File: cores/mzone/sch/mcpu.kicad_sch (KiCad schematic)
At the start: 36 parts

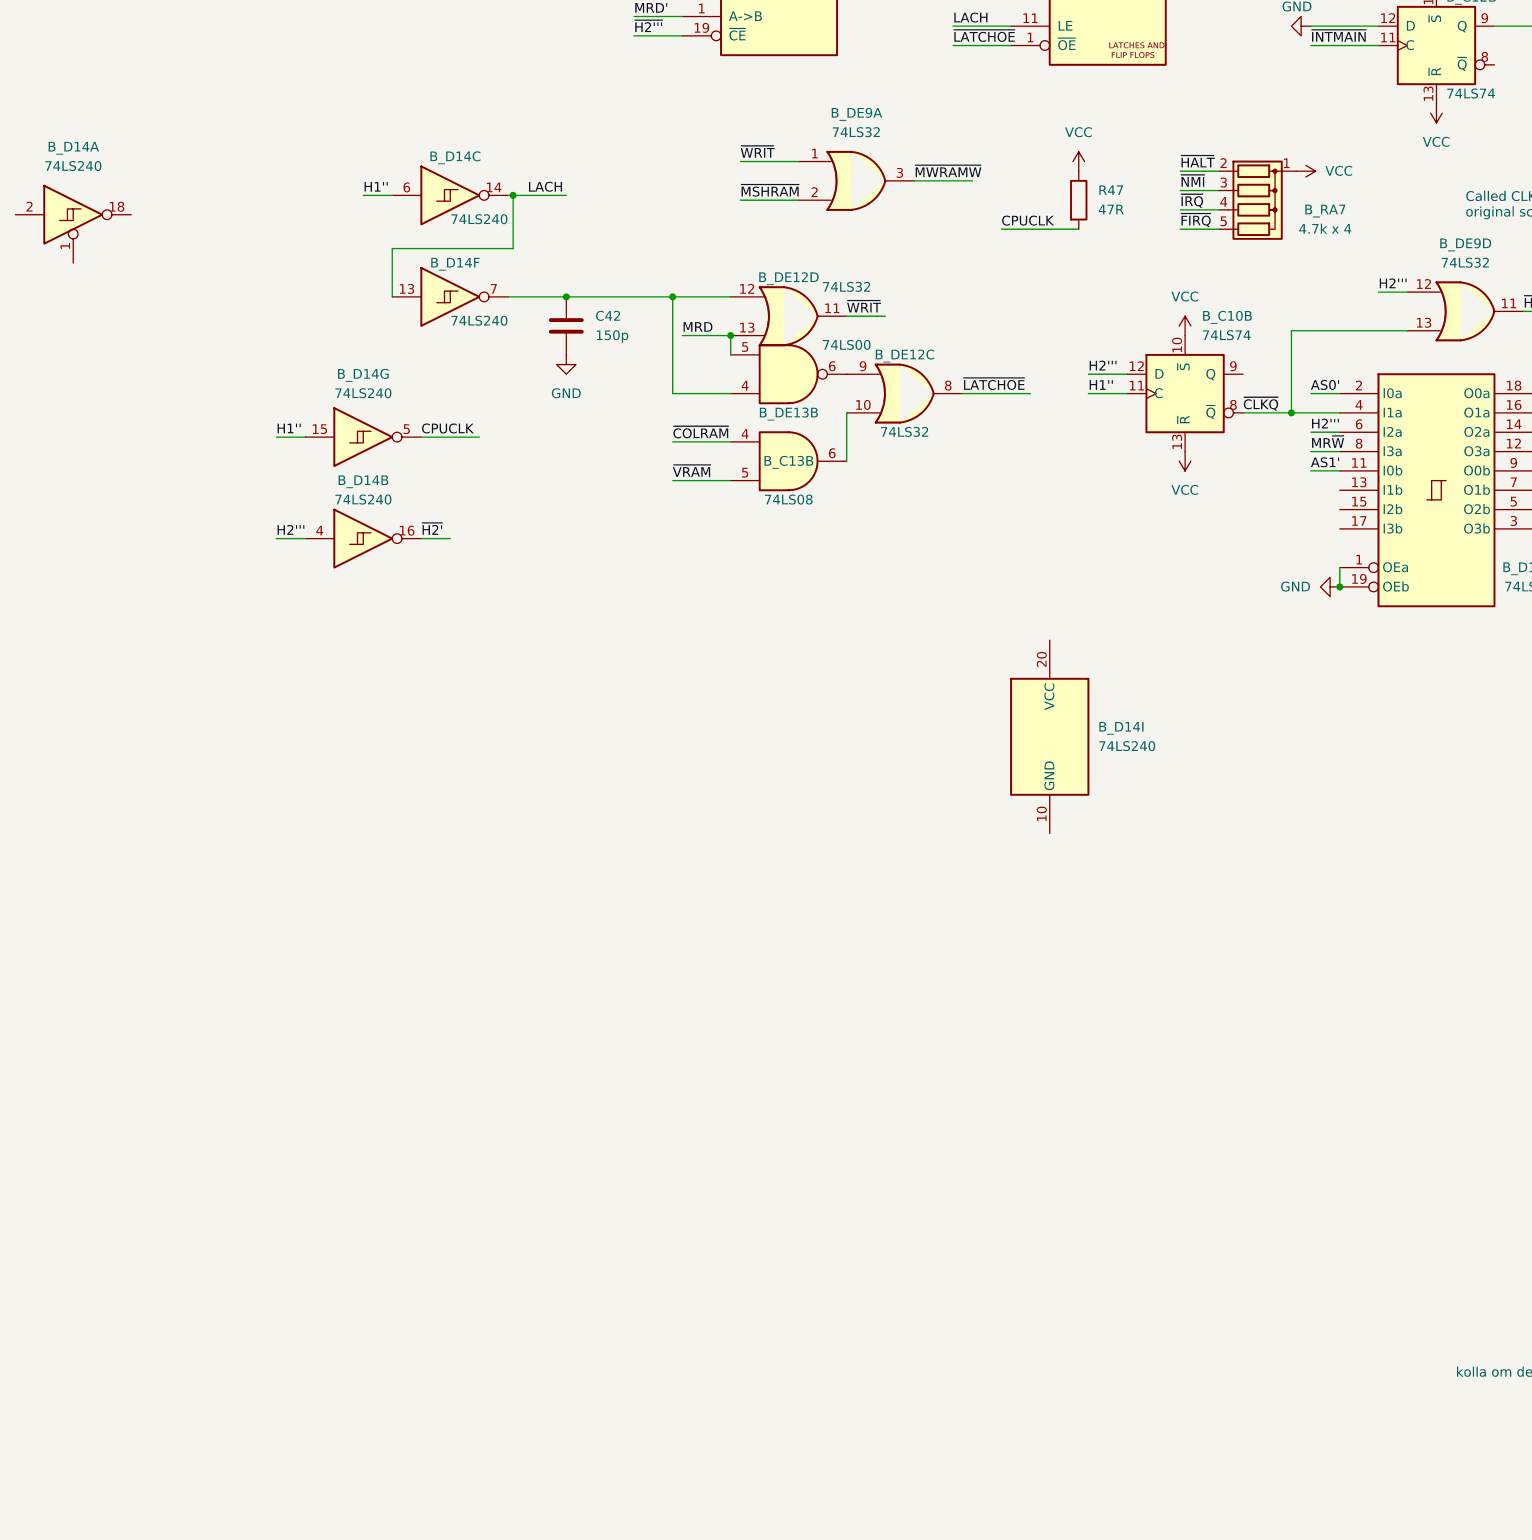
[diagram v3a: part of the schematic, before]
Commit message: mzone core
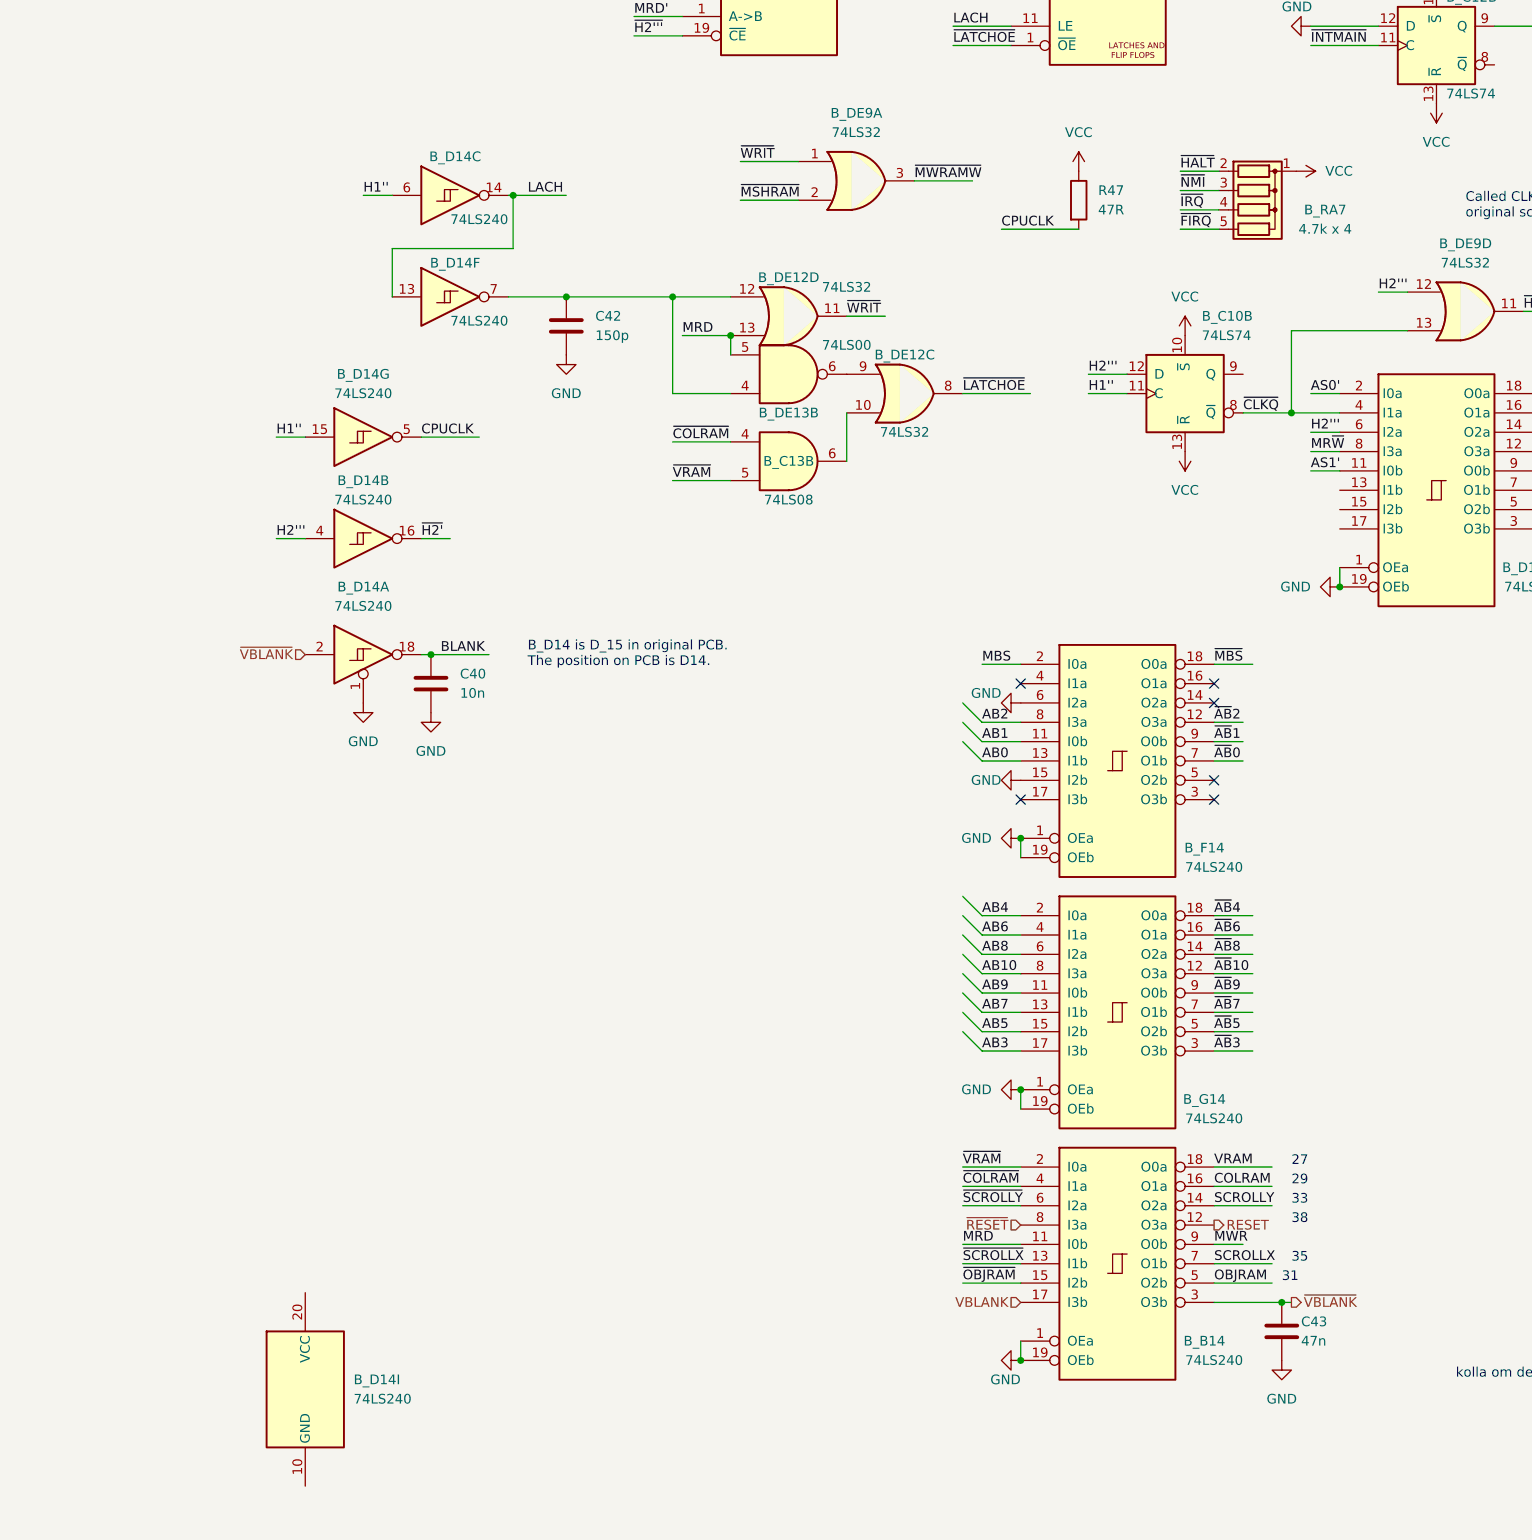
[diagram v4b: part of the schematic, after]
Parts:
- added B_B14, B_F14, B_G14: 74LS240, symbol jt74:74LS240
- added C40: 10n, symbol Device:C
- added C43: 47n, symbol Device:C
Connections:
- net AB0: now also B_F14.13 (I1b)
- net AB1: now also B_F14.11 (I0b)
- net AB10: now also B_G14.8 (I3a)
- net AB2: now also B_F14.8 (I3a)
- net AB3: now also B_G14.17 (I3b)
- net AB4: now also B_G14.2 (I0a)
- net AB5: now also B_G14.15 (I2b)
- net AB6: now also B_G14.4 (I1a)
- net AB7: now also B_G14.13 (I1b)
- net AB8: now also B_G14.6 (I2a)
- net AB9: now also B_G14.11 (I0b)
- net BLANK: now also B_D14.18, C40.1
- net GND: now also B_D14.1, B_B14.1 (OEa), B_B14.19 (OEb), B_F14.1 (OEa), B_F14.15 (I2b), B_F14.19 (OEb), B_F14.6 (I2a), B_G14.1 (OEa), B_G14.19 (OEb), C40.2, C43.2
- net MBS: now also B_F14.2 (I0a)
- net MRD: now also B_B14.11 (I0b)
- net VCC: now also B_B14.20 (VCC), B_F14.20 (VCC), B_G14.20 (VCC)
- net VSS: now also B_B14.10 (VSS), B_F14.10 (VSS), B_G14.10 (VSS)
- net ~{COLRAM}: now also B_B14.4 (I1a)
- net ~{MBS}: now also B_F14.18 (O0a)
- net ~{OBJRAM}: now also B_B14.15 (I2b)
- net ~{RESET}: now also B_B14.8 (I3a)
- net ~{SCROLLX}: now also B_B14.13 (I1b)
- net ~{SCROLLY}: now also B_B14.6 (I2a)
- net ~{VRAM}: now also B_B14.2 (I0a)
- net ~{VBLANK}: now reaches B_D14.2
- net ~{VBLANK}: now also B_B14.3 (O3b), C43.1
- new net COLRAM: B_B14.16 (O1a)
- new net MWR: B_B14.9 (O0b)
- new net OBJRAM: B_B14.5 (O2b)
- new net RESET: B_B14.12 (O3a)
- new net SCROLLX: B_B14.7 (O1b)
- new net SCROLLY: B_B14.14 (O2a)
- new net VBLANK: B_B14.17 (I3b)
- new net VRAM: B_B14.18 (O0a)
- new net ~{AB}0: B_F14.7 (O1b)
- new net ~{AB}1: B_F14.9 (O0b)
- new net ~{AB}10: B_G14.12 (O3a)
- new net ~{AB}2: B_F14.12 (O3a)
- new net ~{AB}3: B_G14.3 (O3b)
- new net ~{AB}4: B_G14.18 (O0a)
- new net ~{AB}5: B_G14.5 (O2b)
- new net ~{AB}6: B_G14.16 (O1a)
- new net ~{AB}7: B_G14.7 (O1b)
- new net ~{AB}8: B_G14.14 (O2a)
- new net ~{AB}9: B_G14.9 (O0b)
- no-connect marks 7 -> 13
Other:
- note added: "27"
- note added: "29"
- note added: "31"
- note added: "33"
- note added: "35"
- note added: "38"
- note added: "B_D14 is D_15 in original PCB. The position on PCB is D14."
- moved on the sheet: B_D14A, B_D14I

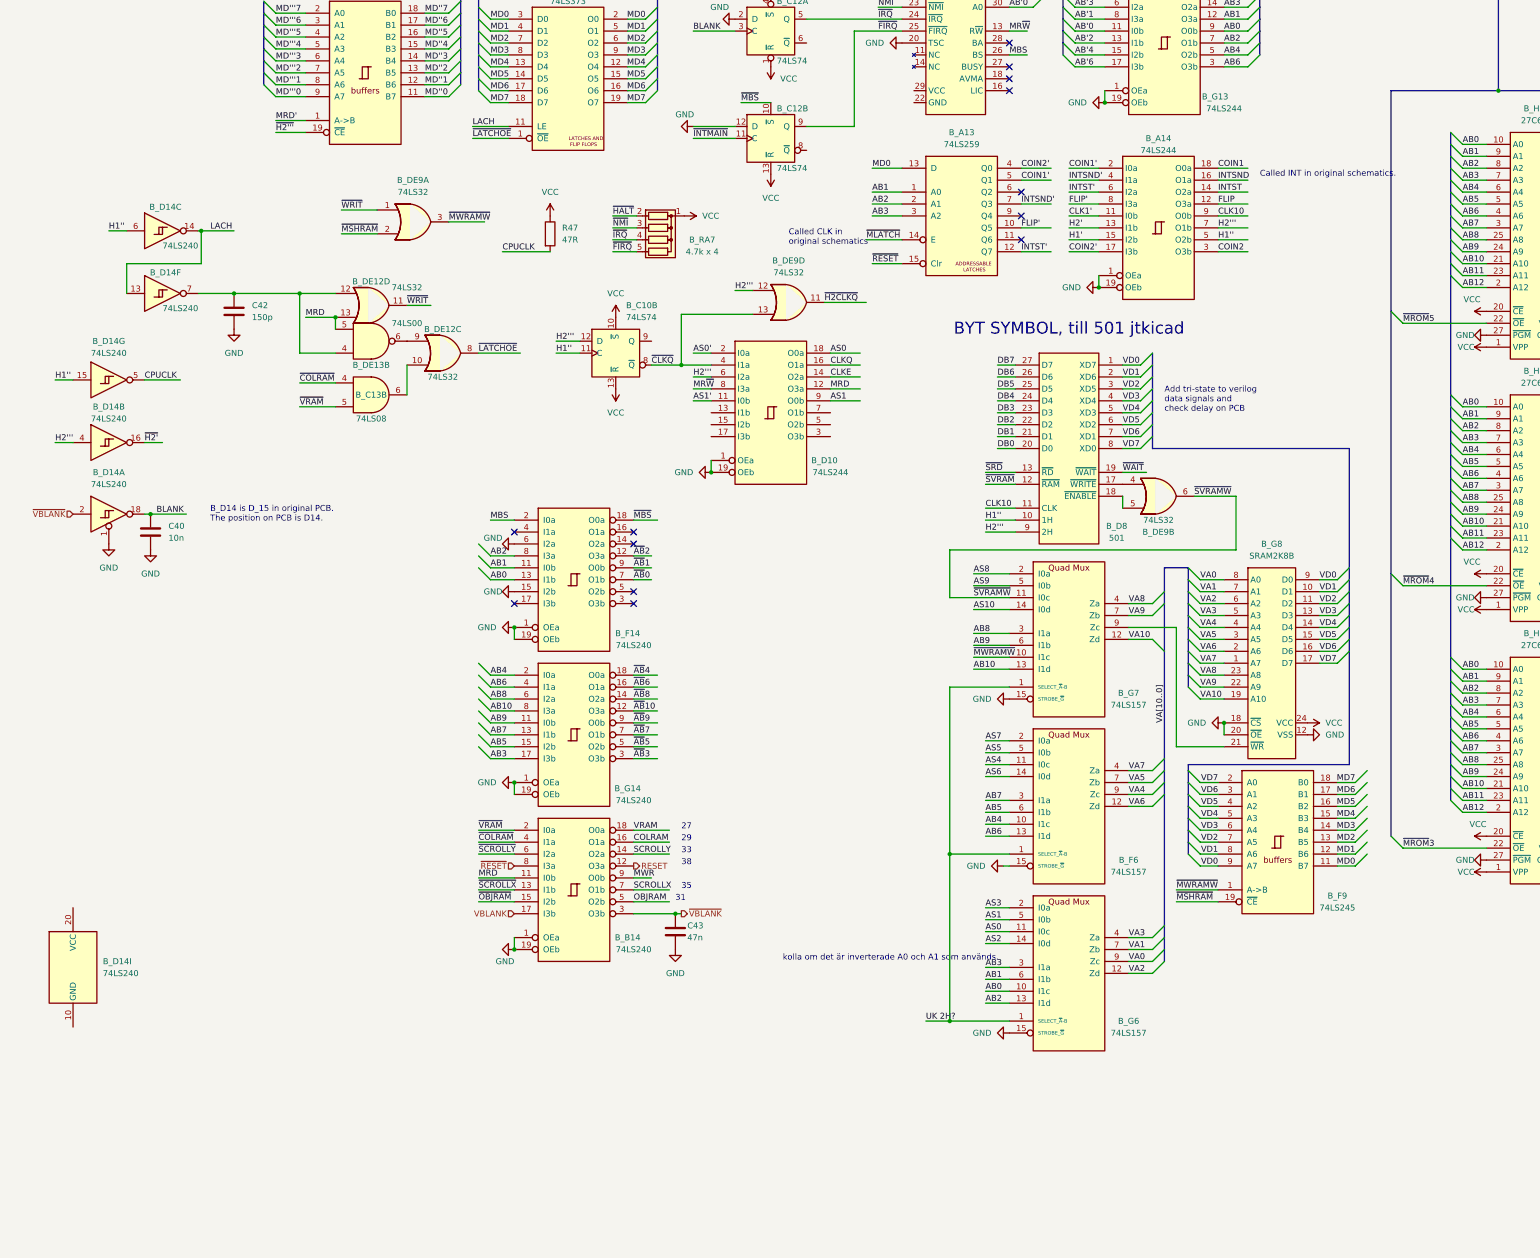
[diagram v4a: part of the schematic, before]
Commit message: mzone core
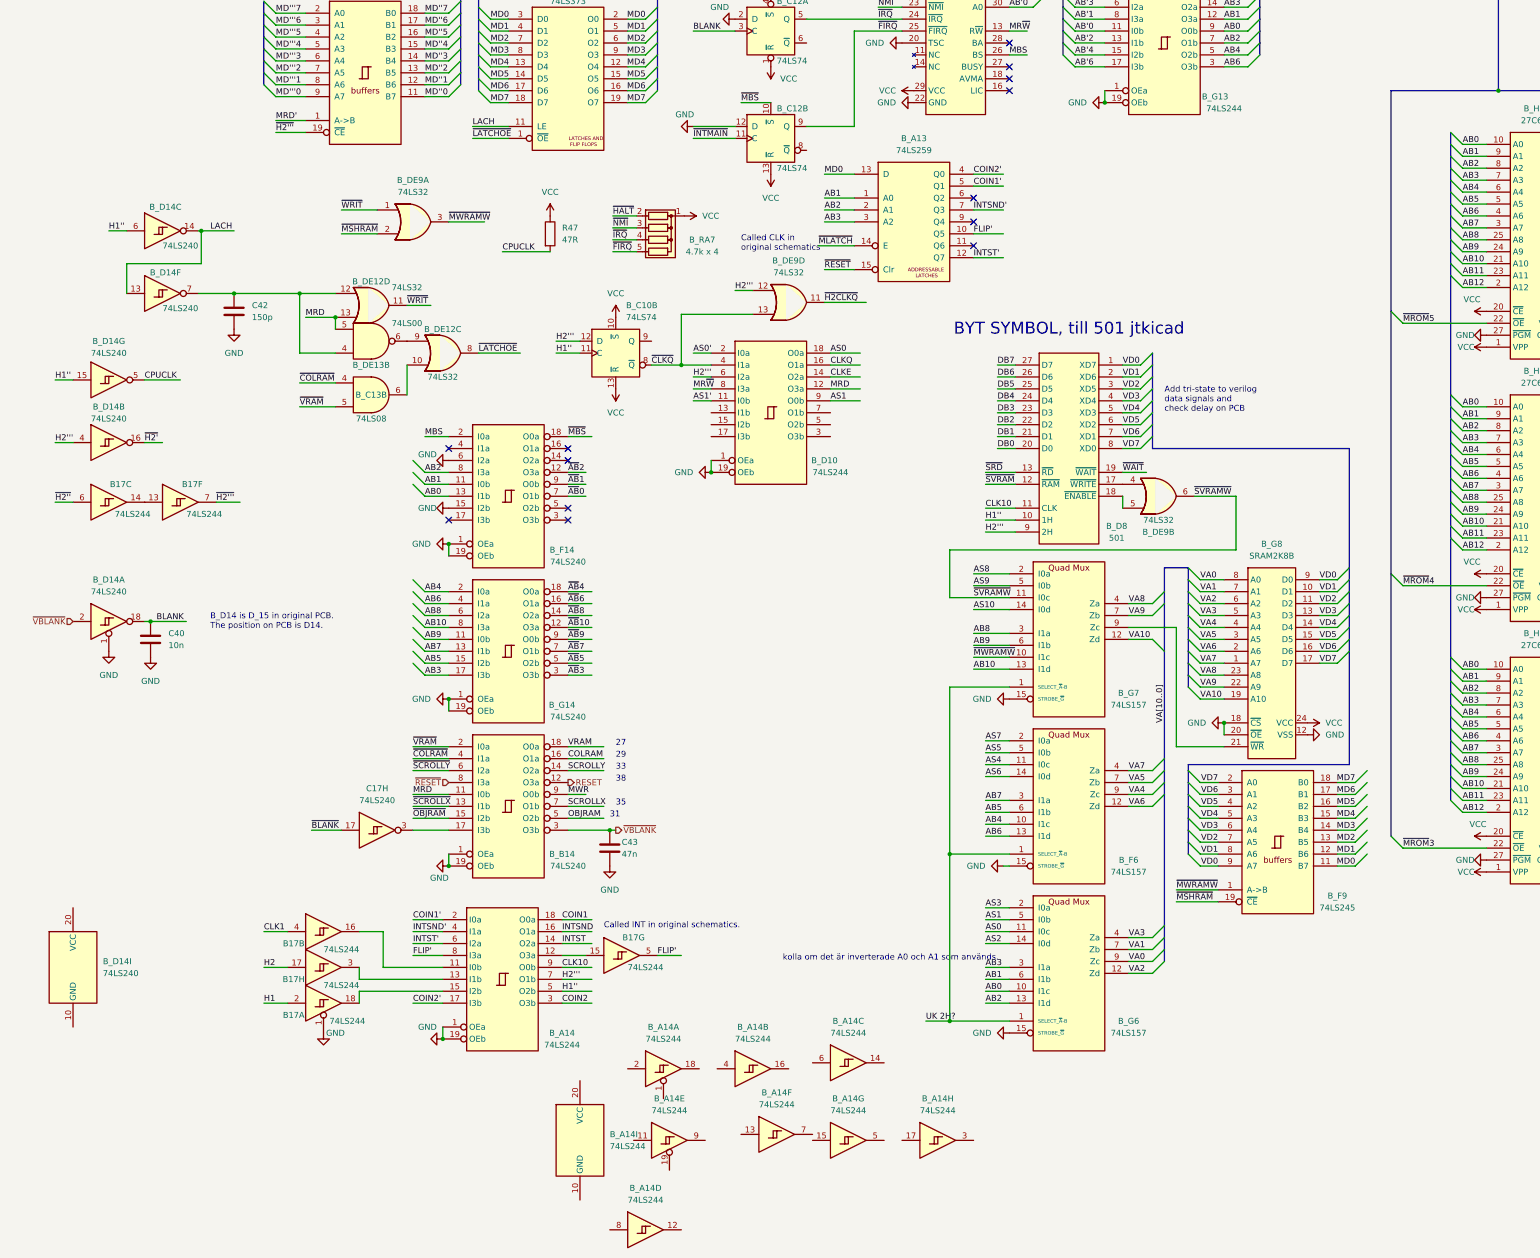
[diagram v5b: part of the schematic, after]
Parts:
- added B17: 74LS244, symbol 74xx:74LS244_Split
- added unit 5 of B_A14
- added unit 2 of B_A14
- added unit 6 of B_A14
- added unit 8 of B_A14
- added unit 7 of B_A14
- added unit 9 of B_A14
- added unit 4 of B_A14
- added unit 3 of B_A14
- added C17: 74LS240, symbol 74xx:74LS240_Split
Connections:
- net FLIP': now also B17.5
- net GND: now also FG12.22 (GND), B17.1
- net VCC: now also FG12.29 (VCC)
- net ~{H2'''}: now also B17.7
- net CLK1': no longer names the net of B_A14.11 (I0b)
- net CLK1': now also B17.16
- net FLIP: no longer names the net of B_A14.12 (O3a)
- net FLIP: now also B17.15
- net H1': no longer names the net of B_A14.15 (I2b)
- net H1': now also B17.18
- net H2': no longer names the net of B_A14.13 (I1b)
- net H2': now also B17.3
- net VBLANK: no longer names the net of B_B14.17 (I3b)
- net VBLANK: now also C17.3
- new net: B17.13, B17.14
- new net CLK1: B17.4
- new net H1: B17.2
- new net H2: B17.17
- new net ~{BLANK}: C17.17
- new net ~{H2''}: B17.6
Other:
- moved on the sheet: B_A13, B_A14, B_B14, B_D14A, B_F14, B_G14, C40, C43

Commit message: mzone core
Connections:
- net COIN1': no longer B_A13.5 (Q1)
- net COIN2': no longer B_A13.4 (Q0)
- net FLIP': no longer B_A13.10 (Q5)
- net GND: now also B_A14.1, B_A14.19
- net INTSND: now also B_A14.9
- net INTSND': no longer B_A13.7 (Q3)
- net at B_A14.11: now also B_A13.7 (Q3)
- net at B_A14.17: now also B_A13.4 (Q0)
- net COIN_CNT'_2: now reaches B_A14.3
- net at B17.15: now also B_A14.12; no longer B_A14.12 (O3a)
- net COIN_CNT'_1: now reaches B_A14.18
- net at B_A14.2: now also B_A13.5 (Q1)
- net at B_A14.8: now also B_A13.10 (Q5)
- no-connect marks 13 -> 19
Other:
- moved on the sheet: B17G, B_A14A, B_A14B, B_A14D, B_A14E, B_A14H, B_A14I
